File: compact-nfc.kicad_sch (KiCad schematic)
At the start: 43 parts, among them J1 Conn_01x10_Pin, J2 Conn_01x07_Pin, Q1 2N7002, Q2 2N7002, U1 ITR9702, U2 PN5321A3HN_C1xx, Y1 Crystal_GND24

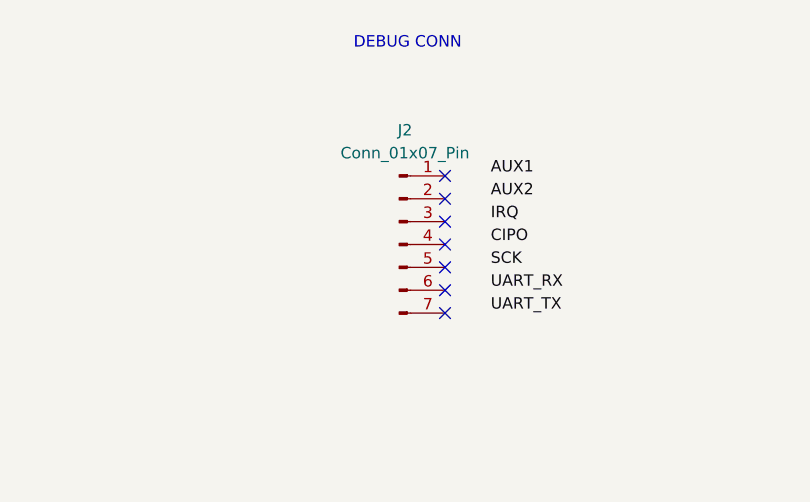
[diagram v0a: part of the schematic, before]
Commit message: Organize silkscreen labels for component assembly identification
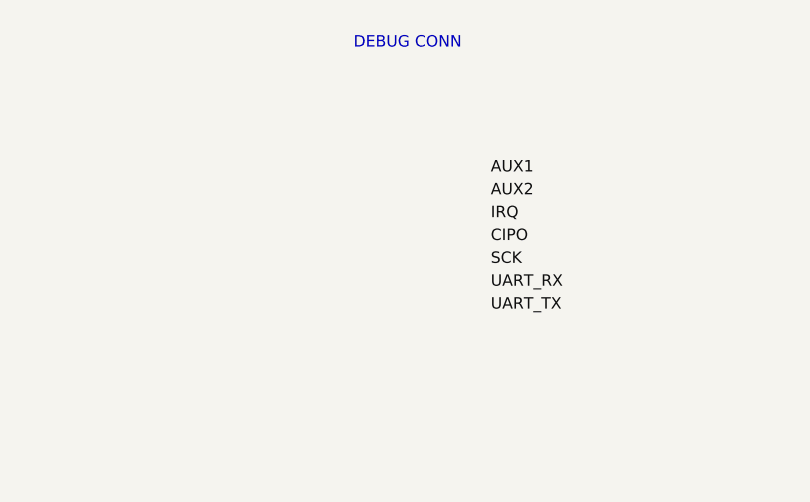
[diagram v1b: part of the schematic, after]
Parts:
- removed J2: Conn_01x07_Pin, Connector_PinHeader_1.27mm:PinHeader_1x07_P1.27mm_Vertical, symbol Connector:Conn_01x07_Pin
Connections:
- no-connect marks 16 -> 9
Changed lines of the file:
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@@
   (no_connect (at 149.86 148.59))
   (no_connect (at 149.86 115.57))
-  (no_connect (at 64.77 48.26))
-  (no_connect (at 64.77 50.8))
-  (no_connect (at 64.77 55.88))
   (no_connect (at 149.86 143.51))
-  (no_connect (at 64.77 45.72))
-  (no_connect (at 64.77 43.18))
   (no_connect (at 149.86 146.05))
-  (no_connect (at 64.77 40.64))
   (no_connect (at 109.22 107.95))
   (no_connect (at 149.86 140.97))
   (no_connect (at 109.22 133.35))
-  (no_connect (at 64.77 53.34))
   (wire (pts (xy 142.24 82.55) (xy 142.24 83.82))
     (stroke (width 0) (type default))
@@
         )
       )
-    )
-  )
-  (symbol (lib_id "Connector:Conn_01x07_Pin") (at 59.69 48.26 0) (unit 1)
-    (in_bom yes) (on_board yes) (dnp no) (fields_autoplaced)
-    (property "Reference" "J2" (at 60.325 35.56 0)
-      (effects (font (size 1.27 1.27)))
-    )
-    (property "Value" "Conn_01x07_Pin" (at 60.325 38.1 0)
-      (effects (font (size 1.27 1.27)))
-    )
-    (property "Footprint" "Connector_PinHeader_1.27mm:PinHeader_1x07_P1.27mm_Vertical" (at 59.69 48.26 0)
-      (effects (font (size 1.27 1.27)) hide)
-    )
-    (property "Datasheet" "~" (at 59.69 48.26 0)
-      (effects (font (size 1.27 1.27)) hide)
-    )
-    (pin "6")
-    (pin "3")
-    (pin "1")
-    (pin "7")
-    (pin "4")
-    (pin "2")
-    (pin "5")
-    (instances
-      (project "compact-nfc"
-        (path "/21d4213f-f9dc-4f6d-96b5-1a03aba56c6c"
-          (reference "J2") (unit 1)
-        )
-      )
